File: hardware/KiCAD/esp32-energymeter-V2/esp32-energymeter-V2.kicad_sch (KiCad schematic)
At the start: 114 parts, among them IC1 ATM90E32AS-AU-R, IC2 NJM2882F33-TE1, IC3 AP63203WU-7, K1 Screw_Terminal_01x06, K2 GSB1C41110SSHR, K3 Qwiic, K4 Conn_01x08, K4 Screw_Terminal_01x06, K5 OLED-A, K5 OLED-B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

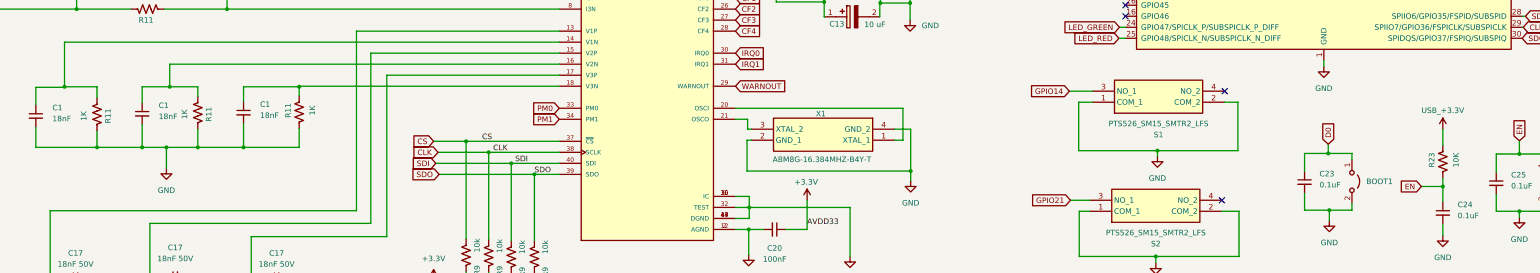
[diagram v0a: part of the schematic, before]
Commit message: minor fix
there were some resistors in the schematic where there was a typo, it was "10K" it should be "10k".
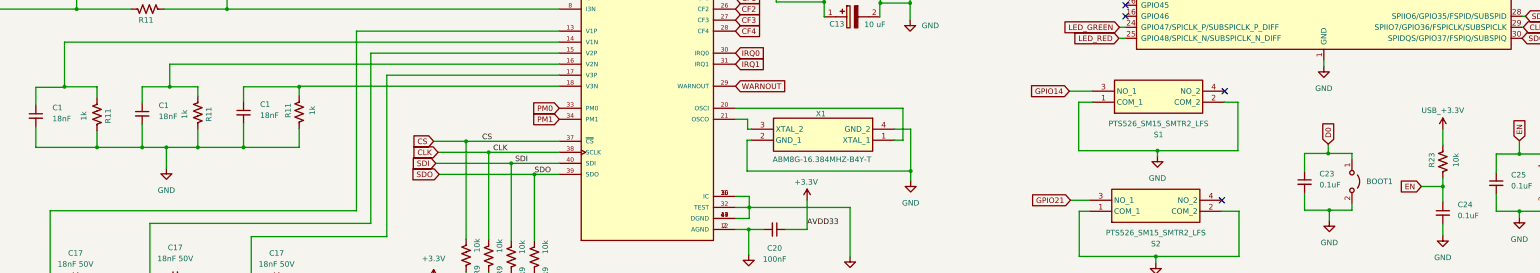
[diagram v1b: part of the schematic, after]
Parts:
- R11: value 1K -> 1k
- R23: value 10K -> 10k
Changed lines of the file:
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@@
       (effects (font (size 1.27 1.27)))
     )
-    (property "Value" "1K" (at 81.915 120.396 90)
+    (property "Value" "1k" (at 81.915 120.396 90)
       (effects (font (size 1.27 1.27)))
     )
@@
       (effects (font (size 1.27 1.27)))
     )
-    (property "Value" "10K" (at 375.031 130.937 90)
+    (property "Value" "10k" (at 375.031 130.937 90)
       (effects (font (size 1.27 1.27)))
     )
@@
       (effects (font (size 1.27 1.27)))
     )
-    (property "Value" "1K" (at 111.379 119.507 90)
+    (property "Value" "1k" (at 111.379 119.507 90)
       (effects (font (size 1.27 1.27)))
     )
@@
       (effects (font (size 1.27 1.27)))
     )
-    (property "Value" "1K" (at 58.674 120.777 90)
+    (property "Value" "1k" (at 58.674 120.777 90)
       (effects (font (size 1.27 1.27)))
     )

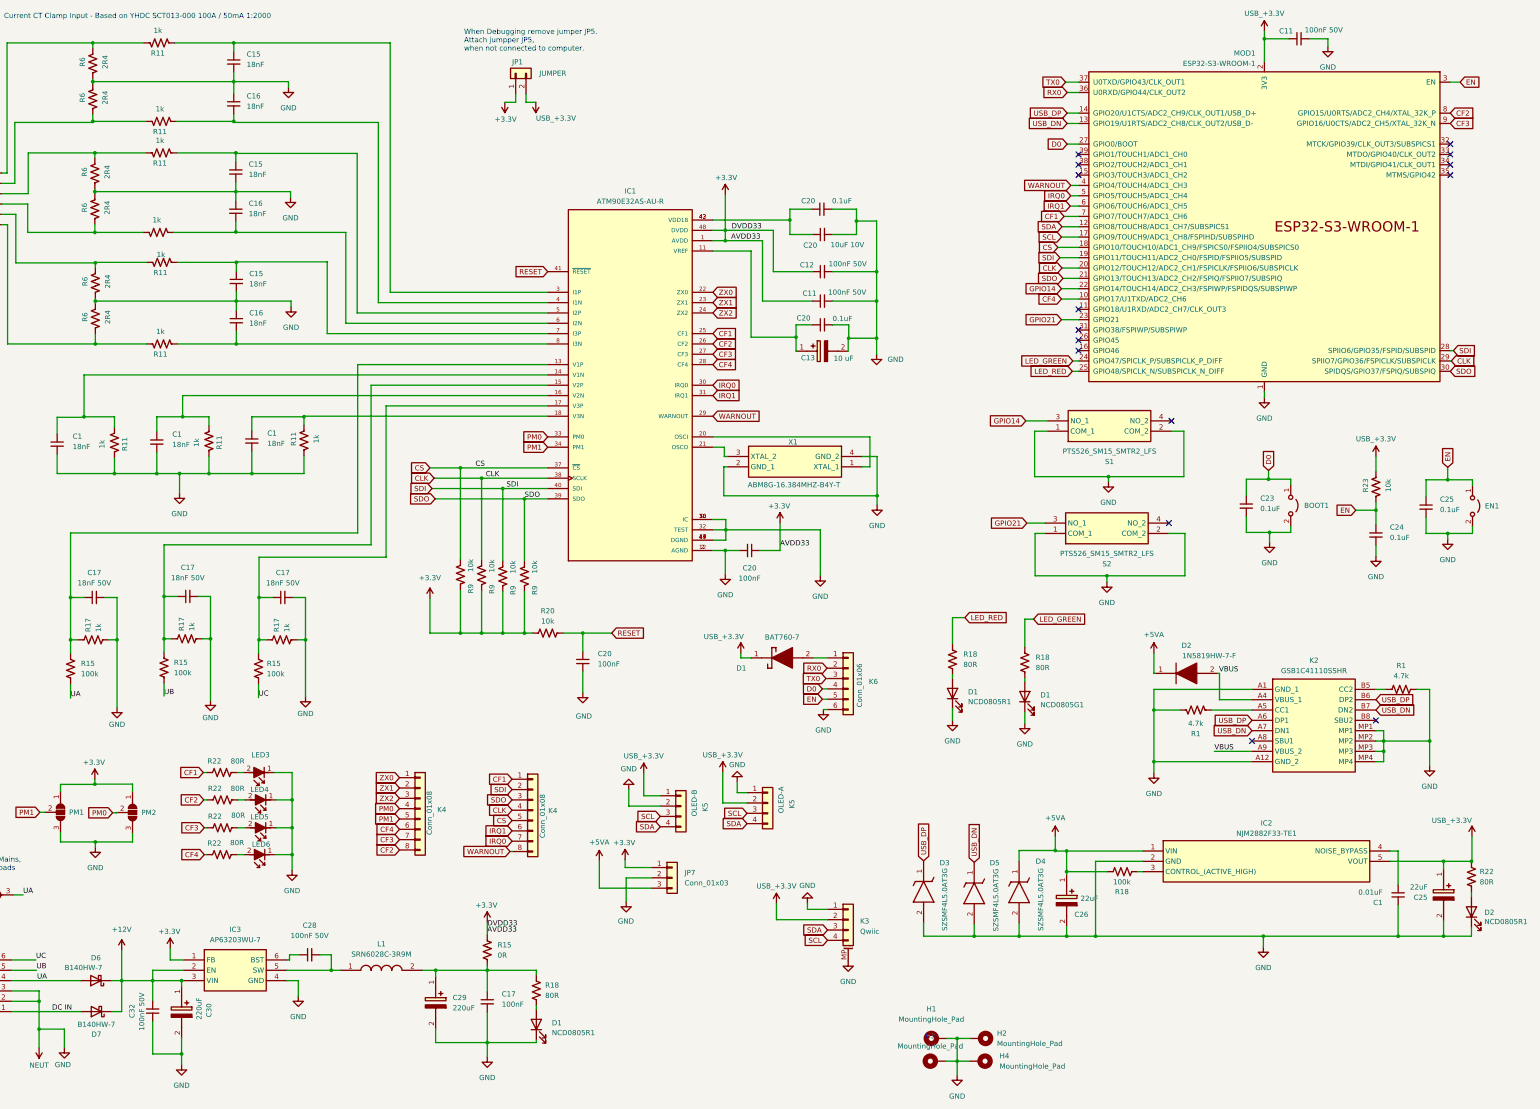
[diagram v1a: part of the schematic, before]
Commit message: updated bom
updated bom lists, mouser and main project bom.
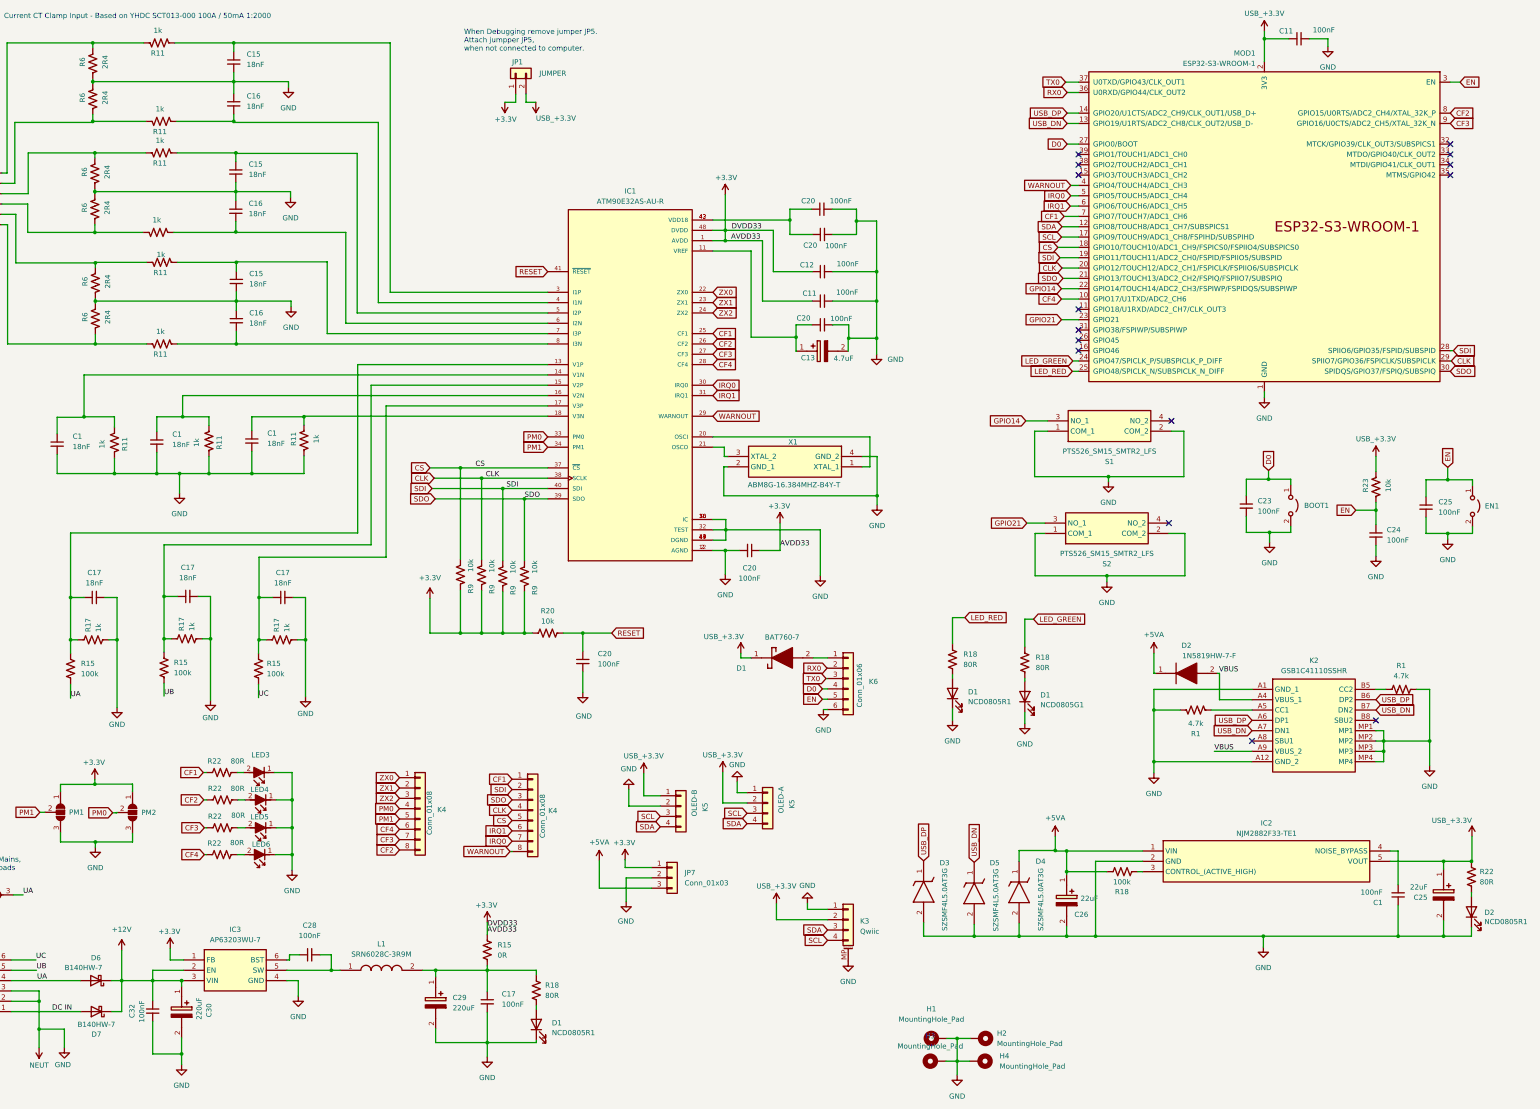
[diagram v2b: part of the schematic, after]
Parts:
- C1: value 0.01uF -> 100nF
- C11, C12, C28, C32: value 100nF 50V -> 100nF; Rating (none) -> 50V
- C13: value 10 uF -> 4.7uF
- C17: value 18nF 50V -> 18nF; Rating (none) -> 50V
- C17: value 18nF 50V -> 18nF; Rating  (none) -> 50V
- C20, C23, C24, C25: value 0.1uF -> 100nF
- C20: value 10uF 10V -> 100nF; Rating (none) -> 10V
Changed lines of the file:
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@@
   (symbol (lib_id "Device:C_Small") (at 371.983 143.129 0) (unit 1)
     (in_bom yes) (on_board yes) (dnp no) (fields_autoplaced)
-    (property "Reference" "C24" (at 375.412 141.224 0)
+    (property "Reference" "C24" (at 374.65 141.8653 0)
       (effects (font (size 1.27 1.27)) (justify left))
     )
-    (property "Value" "0.1uF" (at 375.412 143.764 0)
+    (property "Value" "100nF" (at 374.65 144.4053 0)
       (effects (font (size 1.27 1.27)) (justify left))
     )
@@
       (effects (font (size 1.27 1.27)) (justify left))
     )
-    (property "Value" "0.1uF" (at 243.205 89.916 90)
+    (property "Value" "100nF" (at 243.205 89.916 90)
       (effects (font (size 1.27 1.27)) (justify left))
     )
@@
       (effects (font (size 1.27 1.27)))
     )
-    (property "Value" "10 uF" (at 241.046 99.695 0)
+    (property "Value" "4.7uF" (at 241.046 99.695 0)
       (effects (font (size 1.27 1.27)))
     )
@@
       (effects (font (size 1.27 1.27)))
     )
-    (property "Value" "100nF 50V" (at 242.062 76.454 90)
+    (property "Value" "100nF" (at 242.062 76.454 90)
       (effects (font (size 1.27 1.27)))
     )
@@
       (effects (font (size 1.27 1.27)) hide)
     )
+    (property "Rating" "50V" (at 235.839 78.359 90)
+      (effects (font (size 1.27 1.27)) hide)
+    )
     (pin "1")
     (pin "2")
@@
       (effects (font (size 1.27 1.27)))
     )
-    (property "Value" "100nF 50V" (at 109.728 241.681 90)
+    (property "Value" "100nF" (at 109.728 241.681 90)
       (effects (font (size 1.27 1.27)))
     )
@@
       (effects (font (size 1.27 1.27)) hide)
     )
+    (property "Rating" "50V" (at 109.728 246.38 90)
+      (effects (font (size 1.27 1.27)) hide)
+    )
     (pin "1")
     (pin "2")
@@
       (effects (font (size 1.27 1.27)))
     )
-    (property "Value" "100nF 50V" (at 68.453 260.35 90)
+    (property "Value" "100nF" (at 68.453 260.35 90)
       (effects (font (size 1.27 1.27)))
     )
@@
       (effects (font (size 1.27 1.27)) hide)
     )
+    (property "Rating" " 50V" (at 71.12 260.223 90)
+      (effects (font (size 1.27 1.27)) hide)
+    )
     (pin "1")
     (pin "2")
@@
       (effects (font (size 1.27 1.27)))
     )
-    (property "Value" "100nF 50V" (at 241.935 83.439 90)
+    (property "Value" "100nF" (at 241.935 83.439 90)
       (effects (font (size 1.27 1.27)))
     )
@@
       (effects (font (size 1.27 1.27)) hide)
     )
+    (property "Rating" "50V" (at 235.839 85.598 90)
+      (effects (font (size 1.27 1.27)) hide)
+    )
     (pin "1")
     (pin "2")
@@
       (effects (font (size 1.27 1.27)) (justify left))
     )
-    (property "Value" "10uF 10V" (at 246.126 71.755 90)
+    (property "Value" "100nF" (at 241.935 72.009 90)
       (effects (font (size 1.27 1.27)) (justify left))
     )
@@
       (effects (font (size 1.27 1.27)) hide)
     )
+    (property "Rating" "10V" (at 235.839 69.215 90)
+      (effects (font (size 1.27 1.27)) hide)
+    )
     (pin "1")
     (pin "2")
@@
       (effects (font (size 1.27 1.27)))
     )
-    (property "Value" "18nF 50V" (at 103.1303 154.94 90)
+    (property "Value" "18nF" (at 103.1303 154.94 90)
       (effects (font (size 1.27 1.27)))
     )
@@
       (effects (font (size 1.27 1.27)) hide)
     )
+    (property "Rating" "50V" (at 103.124 158.496 90)
+      (effects (font (size 1.27 1.27)) hide)
+    )
     (pin "1")
     (pin "2")
@@
   (symbol (lib_id "Device:C_Small") (at 384.302 136.271 0) (unit 1)
     (in_bom yes) (on_board yes) (dnp no) (fields_autoplaced)
-    (property "Reference" "C25" (at 387.731 134.366 0)
+    (property "Reference" "C25" (at 387.35 135.0073 0)
       (effects (font (size 1.27 1.27)) (justify left))
     )
-    (property "Value" "0.1uF" (at 387.731 136.906 0)
+    (property "Value" "100nF" (at 387.35 137.5473 0)
       (effects (font (size 1.27 1.27)) (justify left))
     )
@@
   (symbol (lib_id "Device:C_Small") (at 340.106 136.017 0) (unit 1)
     (in_bom yes) (on_board yes) (dnp no) (fields_autoplaced)
-    (property "Reference" "C23" (at 343.535 134.112 0)
+    (property "Reference" "C23" (at 342.9 134.7533 0)
       (effects (font (size 1.27 1.27)) (justify left))
     )
-    (property "Value" "0.1uF" (at 343.535 136.652 0)
+    (property "Value" "100nF" (at 342.9 137.2933 0)
       (effects (font (size 1.27 1.27)) (justify left))
     )
@@
       (effects (font (size 1.27 1.27)))
     )
-    (property "Value" "100nF 50V" (at 359.156 18.923 90)
+    (property "Value" "100nF" (at 359.156 18.923 90)
       (effects (font (size 1.27 1.27)))
     )
@@
       (effects (font (size 1.27 1.27)) hide)
     )
+    (property "Rating" "50V" (at 353.06 21.082 90)
+      (effects (font (size 1.27 1.27)) hide)
+    )
     (pin "1")
     (pin "2")
@@
       (effects (font (size 1.27 1.27)) (justify left))
     )
-    (property "Value" "0.01uF" (at 373.634 231.013 0)
+    (property "Value" "100nF" (at 373.634 231.013 0)
       (effects (font (size 1.27 1.27)) (justify left))
     )
@@
   )
   (symbol (lib_id "Device:C_Small") (at 56.769 158.496 90) (unit 1)
-    (in_bom yes) (on_board yes) (dnp no) (fields_autoplaced)
+    (in_bom yes) (on_board yes) (dnp no)
     (property "Reference" "C17" (at 56.7753 152.4 90)
       (effects (font (size 1.27 1.27)))
     )
-    (property "Value" "18nF 50V" (at 56.7753 154.94 90)
+    (property "Value" "18nF" (at 56.7753 154.94 90)
       (effects (font (size 1.27 1.27)))
     )
@@
       (effects (font (size 1.27 1.27)) hide)
     )
+    (property "Rating" "50V" (at 61.341 154.94 90)
+      (effects (font (size 1.27 1.27)) hide)
+    )
     (pin "1")
     (pin "2")
@@
       (effects (font (size 1.27 1.27)) (justify left))
     )
-    (property "Value" "0.1uF" (at 243.078 60.96 90)
+    (property "Value" "100nF" (at 243.078 60.96 90)
       (effects (font (size 1.27 1.27)) (justify left))
     )
@@
       (effects (font (size 1.27 1.27)))
     )
-    (property "Value" "18nF 50V" (at 79.7623 153.67 90)
+    (property "Value" "18nF" (at 79.7623 153.67 90)
       (effects (font (size 1.27 1.27)))
     )
@@
       (effects (font (size 1.27 1.27)) hide)
     )
+    (property "Rating " "50V" (at 79.756 158.242 90)
+      (effects (font (size 1.27 1.27)) hide)
+    )
